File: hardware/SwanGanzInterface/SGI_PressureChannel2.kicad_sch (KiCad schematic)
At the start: 19 parts, among them U10 OPA2350, U9 INA122D

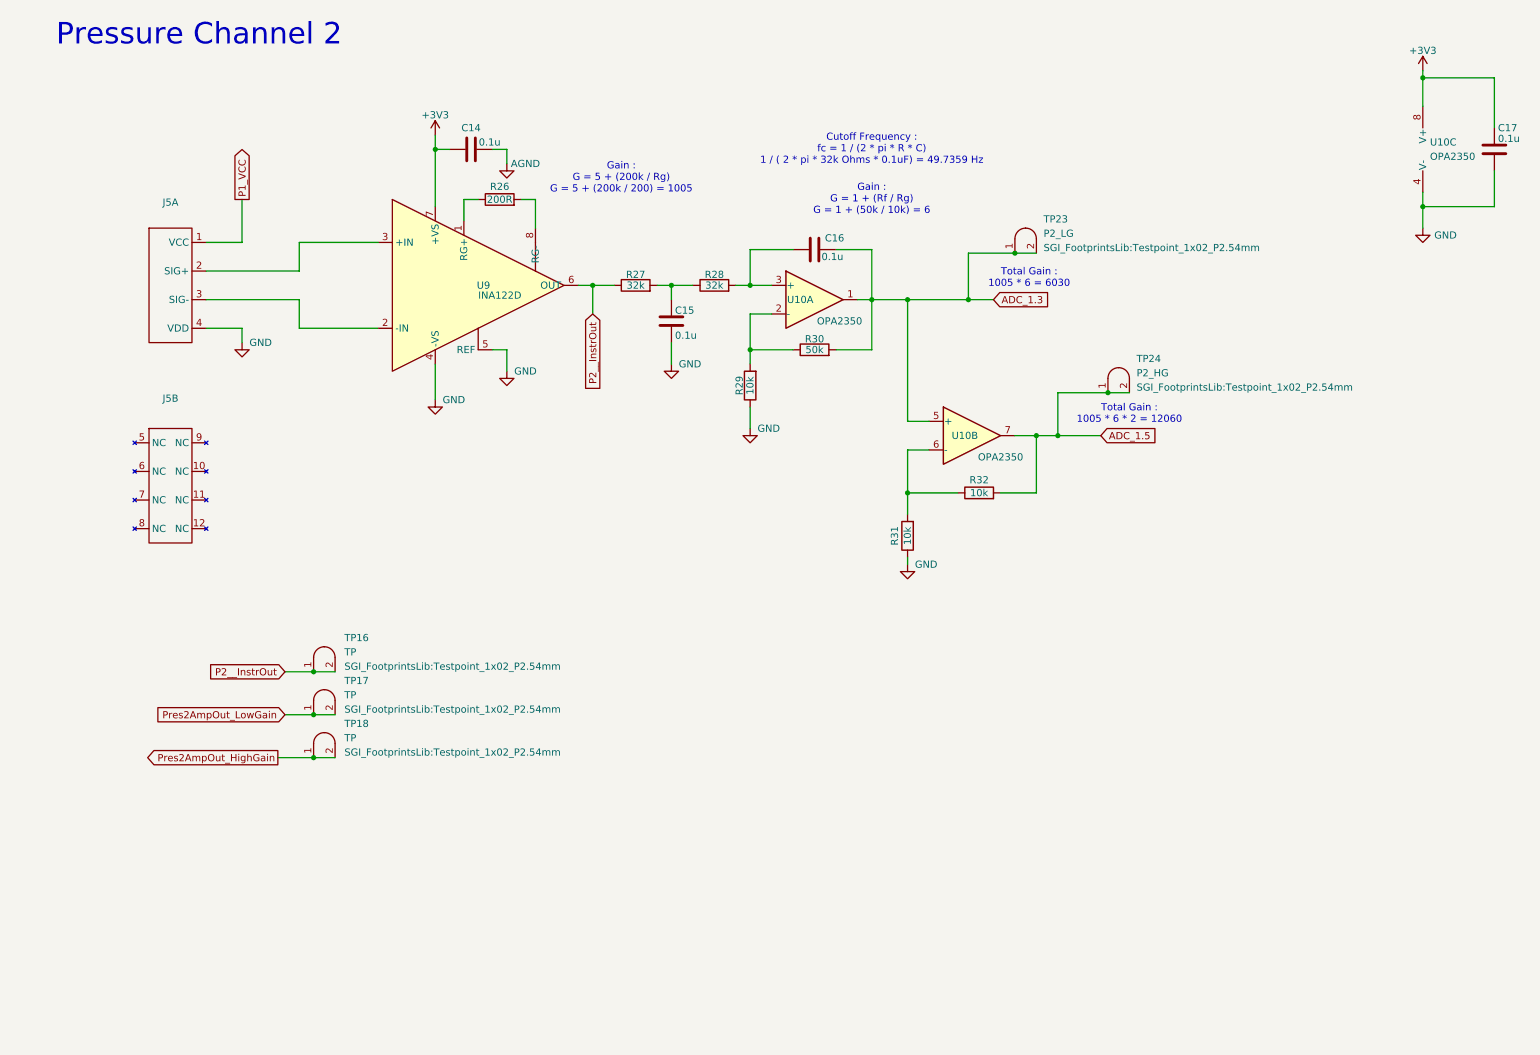
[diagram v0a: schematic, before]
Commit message: Footprints for most parts, added LCD Driver
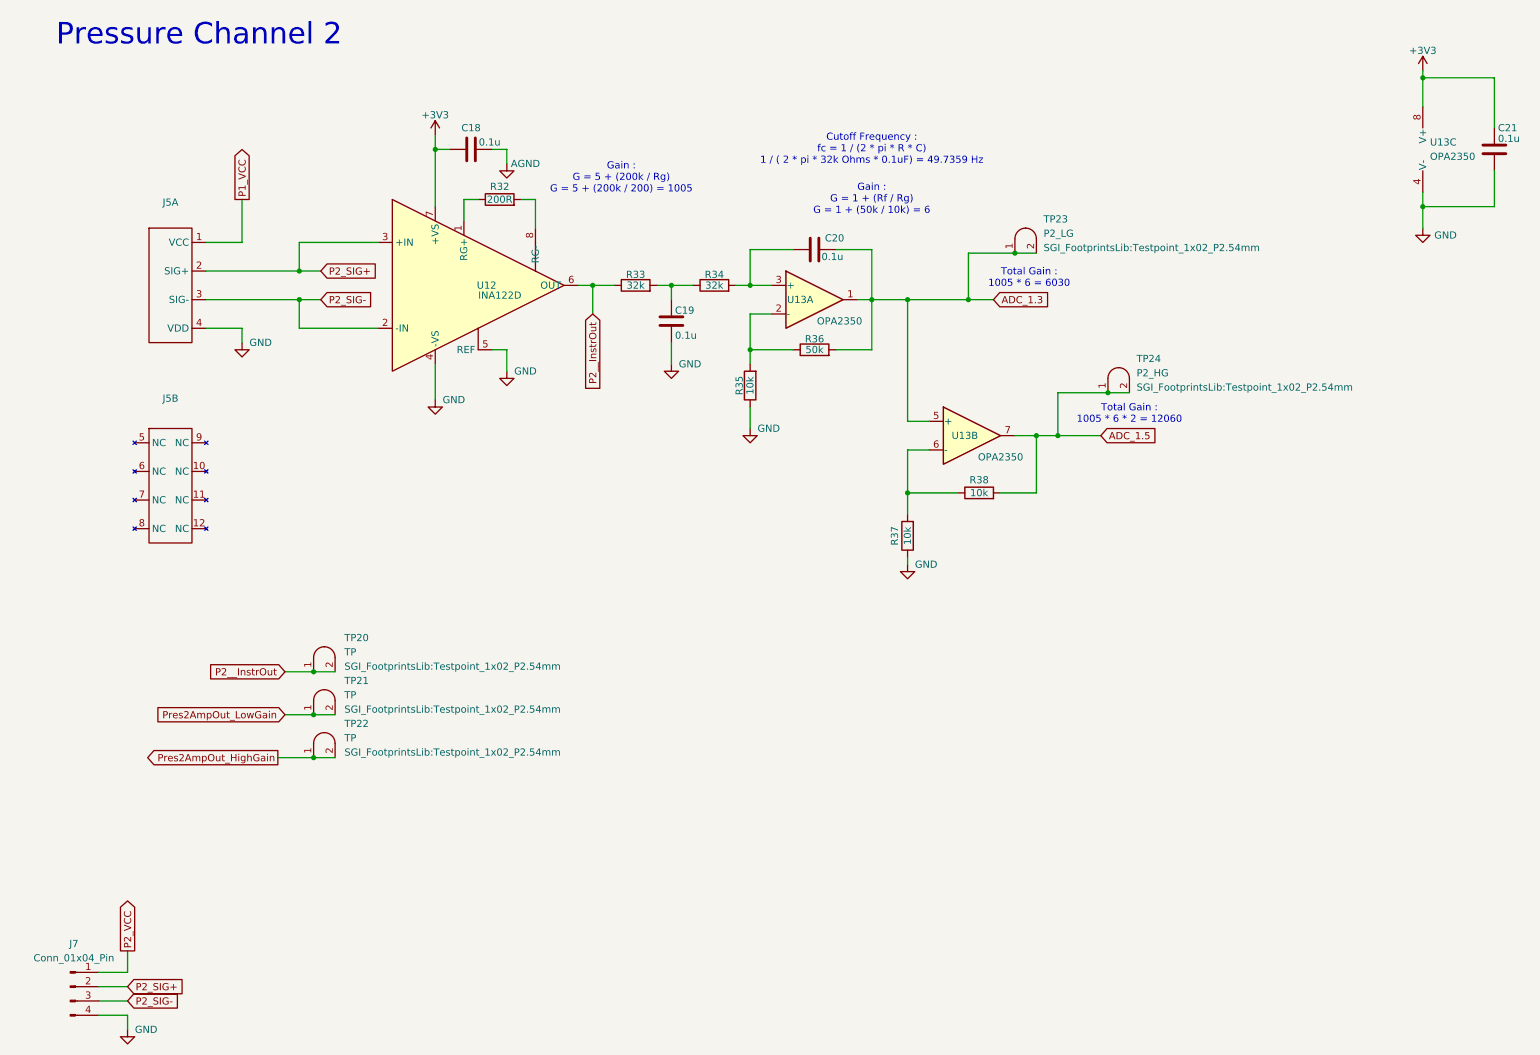
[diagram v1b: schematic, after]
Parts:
- added J7: Conn_01x04_Pin, Connector_PinSocket_2.54mm:PinSocket_1x04_P2.54mm_Vertical, symbol Connector:Conn_01x04_Pin
- R32: renamed from R26; footprint (none) -> Resistor_SMD:R_0603_1608Metric
- R33: renamed from R27; footprint (none) -> Resistor_SMD:R_0603_1608Metric
- R34: renamed from R28; footprint (none) -> Resistor_SMD:R_0603_1608Metric
- R35: renamed from R29; footprint (none) -> Resistor_SMD:R_0603_1608Metric
- R36: renamed from R30; footprint (none) -> Resistor_SMD:R_0603_1608Metric
- R37: renamed from R31; footprint (none) -> Resistor_SMD:R_0603_1608Metric
- R38: renamed from R32; footprint (none) -> Resistor_SMD:R_0603_1608Metric
- renumbered C14 to C18, C15 to C19, C16 to C20, C17 to C21, TP16 to TP20, TP17 to TP21, TP18 to TP22, U9 to U12, U10 to U13
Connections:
- net GND: now also J7.4 (Pin_4)
- net P2_SIG+: now reaches J5.2 (SIG+), U12.3 (+IN)
- net P2_SIG+: now also J7.2 (Pin_2)
- net P2_SIG-: now reaches J5.3 (SIG-), U12.2 (-IN)
- net P2_SIG-: now also J7.3 (Pin_3)
- new net P2_VCC: J7.1 (Pin_1)

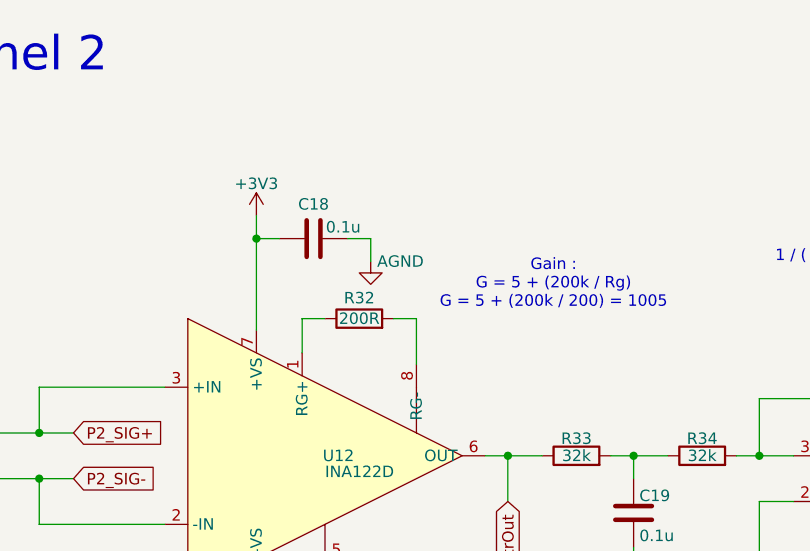
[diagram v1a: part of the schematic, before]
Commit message: Consolidated Grounds
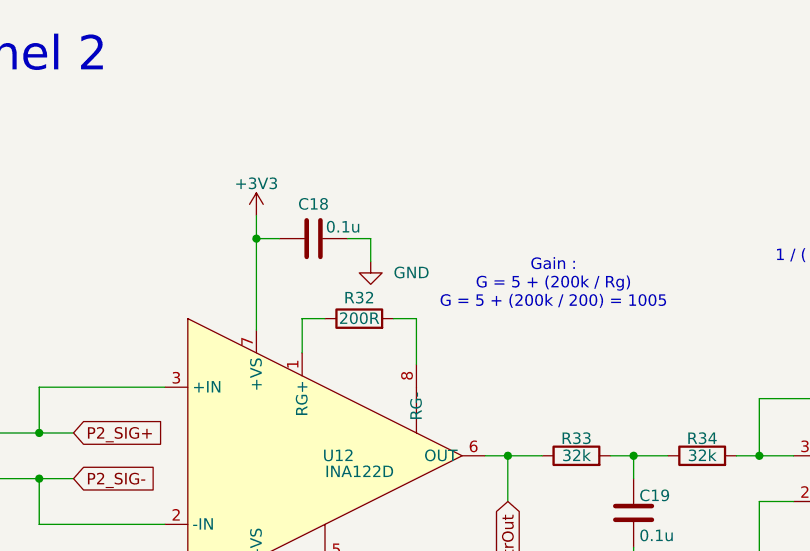
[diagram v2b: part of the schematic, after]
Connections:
- net AGND is gone; now on net GND: C18.1
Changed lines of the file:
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@@
-	)
-	(symbol
-		(lib_id "power:GNDA")
-		(at 96.52 40.64 0)
-		(unit 1)
-		(exclude_from_sim no)
-		(in_bom yes)
-		(on_board yes)
-		(dnp no)
-		(property "Reference" "#PWR065"
-			(at 96.52 46.99 0)
-			(effects
-				(font
-					(size 1.27 1.27)
-				)
-				(hide yes)
-			)
-		)
-		(property "Value" "AGND"
-			(at 99.822 40.64 0)
-			(effects
-				(font
-					(size 1.27 1.27)
-				)
-			)
-		)
-		(property "Footprint" ""
-			(at 96.52 40.64 0)
-			(effects
-				(font
-					(size 1.27 1.27)
-				)
-				(hide yes)
-			)
-		)
-		(property "Datasheet" ""
-			(at 96.52 40.64 0)
-			(effects
-				(font
-					(size 1.27 1.27)
-				)
-				(hide yes)
-			)
-		)
-		(property "Description" "Power symbol creates a global label with name \"GNDA\" , analog ground"
-			(at 96.52 40.64 0)
-			(effects
-				(font
-					(size 1.27 1.27)
-				)
-				(hide yes)
-			)
-		)
-		(pin "1"
-		)
-		(instances
-			(project "SwanGanzInterface"
-				(path "/4e9a6e30-f660-472b-9696-bea1f34b4545/5b443651-3bea-4d19-bd25-a234ca65ad96"
-					(reference "#PWR065")
-					(unit 1)
-				)
-			)
-		)
 	)
 	(symbol
@@
 					(unit 1)
 				)
+			)
+		)
+	)
+	(symbol
+		(lib_id "power:GNDA")
+		(at 96.52 40.64 0)
+		(unit 1)
+		(exclude_from_sim no)
+		(in_bom yes)
+		(on_board yes)
+		(dnp no)
+		(fields_autoplaced yes)
+		(property "Reference" "#PWR065"
+			(at 96.52 46.99 0)
+			(effects
+				(font
+					(size 1.27 1.27)
+				)
+				(hide yes)
+			)
+		)
+		(property "Value" "GND"
+			(at 99.06 41.9099 0)
+			(effects
+				(font
+					(size 1.27 1.27)
+				)
+				(justify left)
+			)
+		)
+		(property "Footprint" ""
+			(at 96.52 40.64 0)
+			(effects
+				(font
+					(size 1.27 1.27)
+				)
+				(hide yes)
+			)
+		)
+		(property "Datasheet" ""
+			(at 96.52 40.64 0)
+			(effects
+				(font
+					(size 1.27 1.27)
+				)
+				(hide yes)
+			)
+		)
+		(property "Description" "Power symbol creates a global label with name \"GNDA\" , analog ground"
+			(at 96.52 40.64 0)
+			(effects
+				(font
+					(size 1.27 1.27)
+				)
+				(hide yes)
+			)
+		)
+		(pin "1"
+		)
+		(instances
+			(project "SwanGanzInterface"
+				(path "/4e9a6e30-f660-472b-9696-bea1f34b4545/5b443651-3bea-4d19-bd25-a234ca65ad96"
+					(reference "#PWR065")
+					(unit 1)
+				)

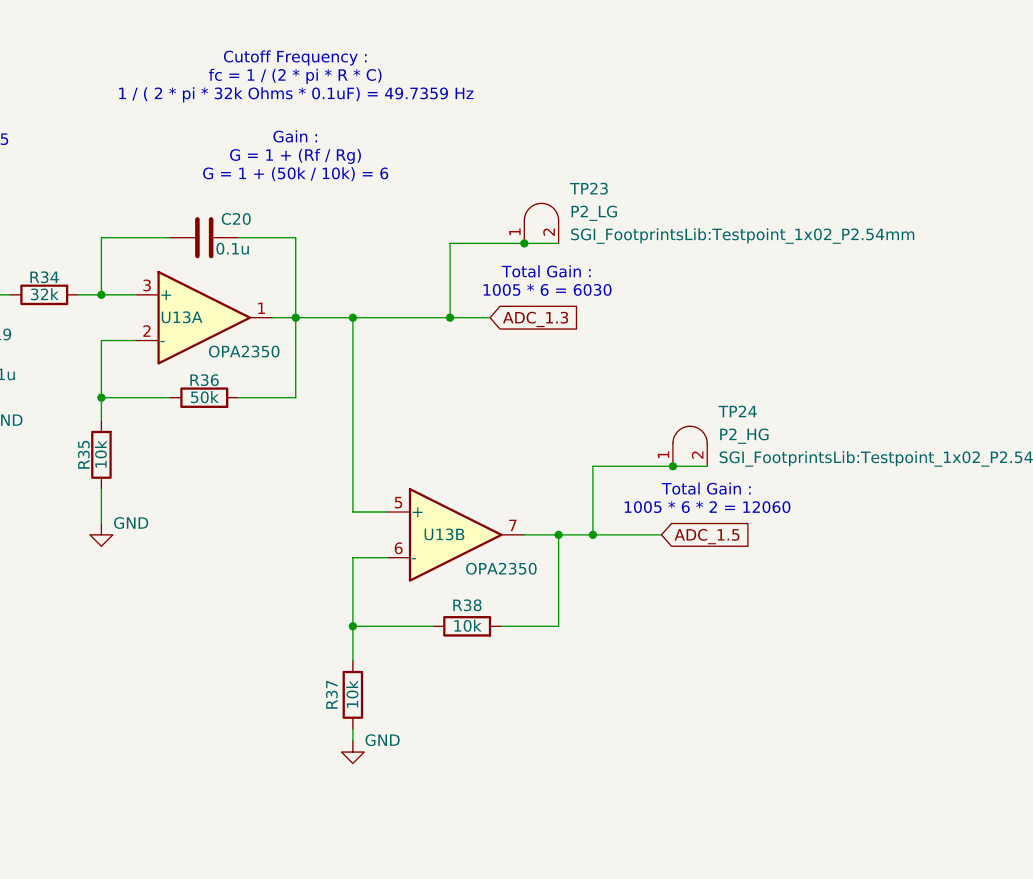
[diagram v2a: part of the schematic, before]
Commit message: Updated Pressure Gain
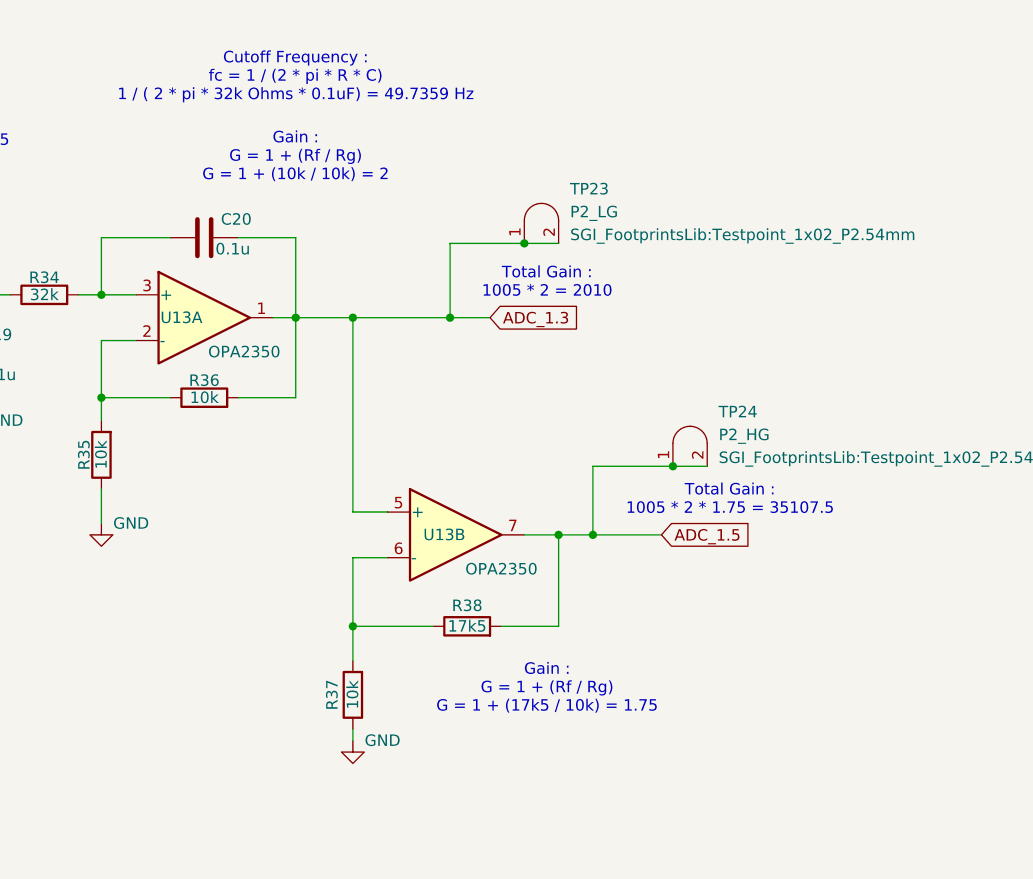
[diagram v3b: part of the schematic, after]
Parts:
- R36: value 50k -> 10k
- R38: value 10k -> 17k5
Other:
- note added: "Gain : G = 1 + (Rf / Rg) G = 1 + (10k / 10k) = 2"
- note added: "Gain : G = 1 + (Rf / Rg) G = 1 + (17k5 / 10k) = 1.75"
- note added: "Total Gain : 1005 * 2 * 1.75 = 35107.5"
- note added: "Total Gain : 1005 * 2 = 2010"
- note removed: "Gain : G = 1 + (Rf / Rg) G = 1 + (50k / 10k) = 6"
- note removed: "Total Gain : 1005 * 6 * 2 = 12060"
- note removed: "Total Gain : 1005 * 6 = 6030"
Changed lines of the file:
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@@
 		(comment 3 "Faculty Mentor - Dr. Valvano")
+	)
+	(text "Gain :\nG = 1 + (Rf / Rg)\nG = 1 + (17k5 / 10k) = 1.75"
+		(exclude_from_sim no)
+		(at 189.23 106.045 0)
+		(effects
+			(font
+				(size 1.27 1.27)
+			)
+		)
 	)
 	(text "Cutoff Frequency :\nfc = 1 / (2 * pi * R * C)\n1 / ( 2 * pi * 32k Ohms * 0.1uF) = 49.7359 Hz"
@@
 		)
 	)
-	(text "Total Gain :\n1005 * 6 * 2 = 12060"
-		(exclude_from_sim no)
-		(at 207.01 85.09 0)
+	(text "Total Gain :\n1005 * 2 * 1.75 = 35107.5"
+		(exclude_from_sim no)
+		(at 209.55 85.09 0)
 		(effects
 			(font
@@
 		)
 	)
-	(text "Gain :\nG = 1 + (Rf / Rg)\nG = 1 + (50k / 10k) = 6"
+	(text "Gain :\nG = 1 + (Rf / Rg)\nG = 1 + (10k / 10k) = 2"
 		(exclude_from_sim no)
 		(at 161.29 46.99 0)
@@
 		)
 	)
-	(text "Total Gain :\n1005 * 6 = 6030"
+	(text "Total Gain :\n1005 * 2 = 2010"
 		(exclude_from_sim no)
 		(at 189.23 60.96 0)
@@
 			)
 		)
-		(property "Value" "50k"
+		(property "Value" "10k"
 			(at 151.13 73.66 90)
 			(effects
@@
 			)
 		)
-		(property "Value" "10k"
+		(property "Value" "17k5"
 			(at 180.34 99.06 90)
 			(effects

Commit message: Started Routing
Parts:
- removed TP21, TP22: TP, SGI_FootprintsLib:Testpoint_1x02_P2.54mm, symbol SGI_SymbolLib:Testpoint
- J5: footprint (none) -> SGI_FootprintsLib:Pressure_Connector
- TP20: value TP -> P2_InstOut
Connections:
- net P1_VCC is gone; now on net P2_VCC: J5.1 (VCC)
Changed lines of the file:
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@@
-	)
-	(junction
-		(at 62.23 138.43)
-		(diameter 0)
-		(color 0 0 0 0)
 	)
 	(junction
@@
 		(color 0 0 0 0)
 	)
-	(junction
-		(at 62.23 146.05)
-		(diameter 0)
-		(color 0 0 0 0)
-	)
 	(wire
 		(pts
@@
 	(wire
 		(pts
-			(xy 55.88 146.05) (xy 62.23 146.05)
-		)
-		(stroke
-			(width 0)
-			(type default)
-		)
-	)
-	(wire
-		(pts
 			(xy 111.76 62.23) (xy 115.57 62.23)
 		)
@@
 	(wire
 		(pts
-			(xy 62.23 146.05) (xy 66.04 146.05)
-		)
-		(stroke
-			(width 0)
-			(type default)
-		)
-	)
-	(wire
-		(pts
 			(xy 190.5 88.9) (xy 190.5 99.06)
 		)
@@
 	(wire
 		(pts
-			(xy 62.23 138.43) (xy 66.04 138.43)
-		)
-		(stroke
-			(width 0)
-			(type default)
-		)
-	)
-	(wire
-		(pts
 			(xy 259.08 25.4) (xy 259.08 30.48)
 		)
@@
 	(wire
 		(pts
-			(xy 57.15 138.43) (xy 62.23 138.43)
-		)
-		(stroke
-			(width 0)
-			(type default)
-		)
-	)
-	(wire
-		(pts
 			(xy 139.7 67.31) (xy 143.51 67.31)
 		)
@@
 			(width 0)
 			(type default)
-		)
-	)
-	(global_label "Pres2AmpOut_LowGain"
-		(shape input)
-		(at 57.15 138.43 180)
-		(fields_autoplaced yes)
-		(effects
-			(font
-				(size 1.27 1.27)
-			)
-			(justify right)
-		)
-		(property "Intersheetrefs" "${INTERSHEET_REFS}"
-			(at 32.9983 138.43 0)
-			(effects
-				(font
-					(size 1.27 1.27)
-				)
-				(justify right)
-				(hide yes)
-			)
 		)
 	)
@@
 		)
 	)
-	(global_label "Pres2AmpOut_HighGain"
-		(shape output)
-		(at 55.88 146.05 180)
-		(fields_autoplaced yes)
-		(effects
-			(font
-				(size 1.27 1.27)
-			)
-			(justify right)
-		)
-		(property "Intersheetrefs" "${INTERSHEET_REFS}"
-			(at 31.0026 146.05 0)
-			(effects
-				(font
-					(size 1.27 1.27)
-				)
-				(justify right)
-				(hide yes)
-			)
-		)
-	)
 	(global_label "P2__InstrOut"
 		(shape input)
@@
 		)
 	)
-	(global_label "P1_VCC"
+	(global_label "P2_VCC"
 		(shape output)
 		(at 49.53 46.99 90)
@@
 			)
 		)
-		(property "Footprint" ""
+		(property "Footprint" "SGI_FootprintsLib:Pressure_Connector"
 			(at 36.83 62.23 0)
 			(effects
@@
 		(fields_autoplaced yes)
 		(property "Reference" "TP20"
-			(at 67.691 124.7773 0)
+			(at 67.31 124.7773 0)
 			(effects
 				(font
@@
 			)
 		)
-		(property "Value" "TP"
-			(at 67.691 127.3173 0)
+		(property "Value" "P2_InstOut"
+			(at 67.31 127.3173 0)
 			(effects
 				(font
@@
 		)
 		(property "Footprint" "SGI_FootprintsLib:Testpoint_1x02_P2.54mm"
-			(at 67.691 129.8573 0)
+			(at 67.31 129.8573 0)
 			(effects
 				(font
@@
 			)
 		)
-		(property "Footprint" ""
+		(property "Footprint" "SGI_FootprintsLib:Pressure_Connector"
 			(at 36.83 97.79 0)
 			(effects
@@
 					(unit 1)
 				)
-			)
-		)
-	)
-	(symbol
-		(lib_id "SGI_SymbolLib:Testpoint")
-		(at 64.135 138.43 0)
-		(unit 1)
-		(exclude_from_sim no)
-		(in_bom yes)
-		(on_board yes)
-		(dnp no)
-		(fields_autoplaced yes)
-		(property "Reference" "TP21"
-			(at 67.691 132.3973 0)
-			(effects
-				(font
-					(size 1.27 1.27)
-				)
-				(justify left)
-			)
-		)
-		(property "Value" "TP"
-			(at 67.691 134.9373 0)
-			(effects
-				(font
-					(size 1.27 1.27)
-				)
-				(justify left)
-			)
-		)
-		(property "Footprint" "SGI_FootprintsLib:Testpoint_1x02_P2.54mm"
-			(at 67.691 137.4773 0)
-			(effects
-				(font
-					(size 1.27 1.27)
-				)
-				(justify left)
-			)
-		)
-		(property "Datasheet" "~"
-			(at 64.135 138.43 0)
-			(effects
-				(font
-					(size 1.27 1.27)
-				)
-				(hide yes)
-			)
-		)
-		(property "Description" "Testpoint"
-			(at 64.135 138.43 0)
-			(effects
-				(font
-					(size 1.27 1.27)
-				)
-				(hide yes)
-			)
-		)
-		(pin "2"
-		)
-		(pin "1"
-		)
-		(instances
-			(project "SwanGanzInterface"
-				(path "/4e9a6e30-f660-472b-9696-bea1f34b4545/5b443651-3bea-4d19-bd25-a234ca65ad96"
-					(reference "TP21")
-					(unit 1)
-				)
-			)
-		)
-	)
-	(symbol
-		(lib_id "SGI_SymbolLib:Testpoint")
-		(at 64.135 146.05 0)
-		(unit 1)
-		(exclude_from_sim no)
-		(in_bom yes)
-		(on_board yes)
-		(dnp no)
-		(fields_autoplaced yes)
-		(property "Reference" "TP22"
-			(at 67.691 140.0173 0)
-			(effects
-				(font
-					(size 1.27 1.27)
-				)
-				(justify left)
-			)
-		)
-		(property "Value" "TP"
-			(at 67.691 142.5573 0)
-			(effects
-				(font
-					(size 1.27 1.27)
-				)
-				(justify left)
-			)
-		)
-		(property "Footprint" "SGI_FootprintsLib:Testpoint_1x02_P2.54mm"
-			(at 67.691 145.0973 0)
-			(effects
-				(font
-					(size 1.27 1.27)
-				)
-				(justify left)
-			)
-		)
-		(property "Datasheet" "~"
-			(at 64.135 146.05 0)
-			(effects
-				(font
-					(size 1.27 1.27)
-				)
-				(hide yes)
-			)
-		)
-		(property "Description" "Testpoint"
-			(at 64.135 146.05 0)
-			(effects
-				(font
-					(size 1.27 1.27)
-				)
-				(hide yes)
-			)
-		)
-		(pin "2"
-		)
-		(pin "1"
-		)
-		(instances
-			(project "SwanGanzInterface"
-				(path "/4e9a6e30-f660-472b-9696-bea1f34b4545/5b443651-3bea-4d19-bd25-a234ca65ad96"
-					(reference "TP22")
-					(unit 1)
-				)
